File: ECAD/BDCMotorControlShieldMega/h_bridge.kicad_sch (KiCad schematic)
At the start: 23 parts, among them J18 Motor Connector, J19 Limit switch, J8 Limit switch, U14 INA180A1, U7 DRV8870DDA

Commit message: Progressed ECAD.
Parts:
- added C1: 0.1uC, Capacitor_SMD:C_0805_2012Metric_Pad1.18x1.45mm_HandSolder, symbol Device:C
- added U1: 74HC2G08, Package_SO:TSSOP-8_3x3mm_P0.65mm, symbol 74xGxx:74LVC2G08
- renumbered C27 to C10, C38 to C2, C31 to C3, C34 to C4, C36 to C5, C41 to C6, C1 to C7, C33 to C8, C15 to C9, J18 to J10, J19 to J8, J8 to J9, R42 to R1, R43 to R2, R47 to R3, R1 to R4, R39 to R5, R3 to R6, R40 to R7, R31 to R8, R2 to R9, U7 to U2, U14 to U3
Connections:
- net +5V: now also C1.1, U1.8 (VCC), U1.8 (VCC)
- net GND: now also C1.2, U1.4 (GND), U1.4 (GND)
- net PWM1: now also U1.2; no longer U2.3 (IN1)
- net PWM2: now also U1.6; no longer U2.2 (IN2)
- new net: U1.3, U2.2 (IN2)
- new net: U1.7, U2.3 (IN1)
- new net ENABLE_PWM: U1.1, U1.5
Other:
- moved on the sheet: C10, C2, C3, C4, C5, C6, C7, C8, C9, J10, J8, J9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

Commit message: Progressed ECAD.
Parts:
- added U17: 74AHC14, Package_SO:TSSOP-14_4.4x5mm_P0.65mm, symbol 74xx:74HC14
- added U21: 74AHC2G125, Package_SO:TSSOP-8_3x3mm_P0.65mm, symbol 74xGxx:74AUC2G125
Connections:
- net ENCODER_A: now also U21.3; no longer C7.1, R4.1
- net ENCODER_B: now also U21.6; no longer C10.1, R9.1
- net GND: now also U17.7 (GND), U21.4 (GND)
- net LIM1: now also U17.6; no longer C8.1, R5.1
- net LIM2: now also U17.8; no longer C9.1, R6.1
- new net: C8.1, R5.1, U17.5
- new net: C10.1, R9.1, U17.1
- new net: U17.4, U21.2
- new net: U17.12, U21.5
- new net: C9.1, R6.1, U17.9
- new net: U17.10, U17.13
- new net: C7.1, R4.1, U17.11
- new net: U17.2, U17.3
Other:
- moved on the sheet: C10, C3, C4, C5, C7, C8, C9, J8, J9, R4, R5, R6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

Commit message: Progressed ECAD.
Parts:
- removed U1: 74HC2G08, Package_SO:TSSOP-8_3x3mm_P0.65mm, symbol 74xGxx:74LVC2G08
- added C13, C4: 100nC, Capacitor_SMD:C_0805_2012Metric, symbol Device:C
- added U4: 74AHC2G08, Package_SO:TSSOP-8_3x3mm_P0.65mm, symbol 74xGxx:74AUC2G08
- C10: renamed from C4; footprint Capacitor_SMD:C_1210_3225Metric_Pad1.33x2.70mm_HandSolder -> Capacitor_SMD:C_1210_3225Metric
- C12: renamed from C6; value 0.1uC -> 100nC; footprint Capacitor_SMD:C_0805_2012Metric_Pad1.18x1.45mm_HandSolder -> Capacitor_SMD:C_0805_2012Metric; MPN CC0805KRX7R8BB104 -> C0805F104K5RACAUTO
- C14: renamed from C8; MPN (none) -> C0805F104K5RACAUTO
- C15: renamed from C9; MPN (none) -> C0805F104K5RACAUTO
- C5: renamed from C1; value 0.1uC -> 100nC; footprint Capacitor_SMD:C_0805_2012Metric_Pad1.18x1.45mm_HandSolder -> Capacitor_SMD:C_0805_2012Metric; MPN CC0805KRX7R8BB104 -> C0805F104K5RACAUTO
- C6: renamed from C2; value 0.1uC -> 100nC; footprint Capacitor_SMD:C_0805_2012Metric_Pad1.18x1.45mm_HandSolder -> Capacitor_SMD:C_0805_2012Metric; MPN CC0805KRX7R8BB104 -> C0805F104K5RACAUTO
- C7: renamed from C3; value 0.1uC -> 100nC; footprint Capacitor_SMD:C_0805_2012Metric_Pad1.18x1.45mm_HandSolder -> Capacitor_SMD:C_0805_2012Metric; MPN CC0805KRX7R8BB104 -> C0805F104K5RACAUTO
- C8: renamed from C7; footprint Capacitor_SMD:C_0402_1005Metric -> Capacitor_SMD:C_0805_2012Metric
- C9: renamed from C10; footprint Capacitor_SMD:C_0402_1005Metric -> Capacitor_SMD:C_0805_2012Metric
- R10: renamed from R2; footprint Resistor_SMD:R_0805_2012Metric_Pad1.20x1.40mm_HandSolder -> Resistor_SMD:R_0805_2012Metric; MPN RC0805FR-0710KL -> RC0805JR-0710KL
- R11: renamed from R4; footprint Resistor_SMD:R_0402_1005Metric -> Resistor_SMD:R_0805_2012Metric; MPN RC0402FR-071KL -> AC0805FR-7W1KL
- R12: renamed from R9; footprint Resistor_SMD:R_0402_1005Metric -> Resistor_SMD:R_0805_2012Metric; MPN RC0402FR-071KL -> AC0805FR-7W1KL
- R14: renamed from R5; footprint Capacitor_SMD:C_0805_2012Metric -> Resistor_SMD:R_0805_2012Metric; MPN (none) -> RC0805JR-0710KL
- R15: renamed from R6; footprint Capacitor_SMD:C_0805_2012Metric -> Resistor_SMD:R_0805_2012Metric; MPN (none) -> RC0805JR-0710KL
- R16: renamed from R7; footprint Capacitor_SMD:C_0805_2012Metric -> Resistor_SMD:R_0805_2012Metric; MPN (none) -> RC0805JR-0710KL
- R17: renamed from R8; footprint Capacitor_SMD:C_0805_2012Metric -> Resistor_SMD:R_0805_2012Metric; MPN (none) -> RC0805JR-0710KL
- R9: renamed from R1; footprint Resistor_SMD:R_0805_2012Metric_Pad1.20x1.40mm_HandSolder -> Resistor_SMD:R_0805_2012Metric; MPN RC0805FR-0710KL -> RC0805JR-0710KL
- renumbered C5 to C11, J8 to J10, J9 to J11, J10 to J9, R3 to R13, U21 to U3, U17 to U5, U2 to U6, U3 to U7
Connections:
- net +5V: now also U3.8 (VCC), U5.14 (VCC), C13.1, C4.1, U4.8 (VCC)
- net ENABLE_PWM: now also U4.1, U4.5
- net GND: now also C13.2, C4.2, U4.4 (GND)
- net PWM1: now also U4.2
- net PWM2: now also U4.6
- net ~{ENABLE_ENCODER}: now reaches U3.1
- net ~{ENABLE_ENCODER}: now also U3.7
- net at U6.2 (IN2): now also U4.3
- net at U6.3 (IN1): now also U4.7
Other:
- moved on the sheet: C10, C11, C12, C5, C6, C7, C8, C9, J9, R10, R11, R12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

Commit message: Progressed ECAD.
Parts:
- added C14: 100nC, Capacitor_SMD:C_0805_2012Metric, symbol Device:C
- added L1: 10uL, Inductor_SMD:L_0805_2012Metric, symbol Device:L
- renumbered C8 to C10, C9 to C11, C11 to C12, C12 to C13, C13 to C15, C14 to C16, C15 to C17, C4 to C5, C5 to C6, C6 to C7, C7 to C8, C10 to C9
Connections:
- net +5V: now also L1.1; no longer U7.5 (V+)
- net GND: now also C14.2
- new net: C14.1, L1.2, U7.5 (V+)
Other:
- moved on the sheet: C12, C13, C6, C7, C8, C9, R10, R13, R9, U4A, U4B, U4C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

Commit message: Progressed ECAD.
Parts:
- C12, C13, C14, C15, C16, C17, C5, C6, C7, C8, C9, R10, R14, R15, R16, R17, R9: Status (none) -> OK
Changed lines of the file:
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@@
 			)
 		)
+		(property "Status" "OK"
+			(at 27.94 147.32 0)
+			(effects
+				(font
+					(size 1.27 1.27)
+				)
+				(hide yes)
+			)
+		)
 		(pin "1"
 		)
@@
 			)
 		)
+		(property "Status" "OK"
+			(at 160.02 49.53 0)
+			(effects
+				(font
+					(size 1.27 1.27)
+				)
+				(hide yes)
+			)
+		)
 		(pin "1"
 		)
@@
 			)
 		)
+		(property "Status" "OK"
+			(at 191.77 118.11 0)
+			(effects
+				(font
+					(size 1.27 1.27)
+				)
+				(hide yes)
+			)
+		)
 		(pin "1"
 		)
@@
 			)
 		)
+		(property "Status" "OK"
+			(at 238.76 66.04 90)
+			(effects
+				(font
+					(size 1.27 1.27)
+				)
+				(hide yes)
+			)
+		)
 		(pin "2"
 		)
@@
 			)
 		)
+		(property "Status" "OK"
+			(at 88.9 83.82 0)
+			(effects
+				(font
+					(size 1.27 1.27)
+				)
+				(hide yes)
+			)
+		)
 		(pin "1"
 		)
@@
 			)
 		)
+		(property "Status" "OK"
+			(at 247.65 60.96 0)
+			(effects
+				(font
+					(size 1.27 1.27)
+				)
+				(hide yes)
+			)
+		)
 		(pin "2"
 		)
@@
 			)
 		)
+		(property "Status" "OK"
+			(at 149.86 49.53 0)
+			(effects
+				(font
+					(size 1.27 1.27)
+				)
+				(hide yes)
+			)
+		)
 		(pin "1"
 		)
@@
 			)
 		)
+		(property "Status" "OK"
+			(at 238.76 33.02 90)
+			(effects
+				(font
+					(size 1.27 1.27)
+				)
+				(hide yes)
+			)
+		)
 		(pin "2"
 		)
@@
 			)
 		)
+		(property "Status" "OK"
+			(at 88.9 73.66 0)
+			(effects
+				(font
+					(size 1.27 1.27)
+				)
+				(hide yes)
+			)
+		)
 		(pin "1"
 		)
@@
 			)
 		)
+		(property "Status" "OK"
+			(at 115.57 29.21 0)
+			(effects
+				(font
+					(size 1.27 1.27)
+				)
+				(hide yes)
+			)
+		)
 		(pin "1"
 		)
@@
 			)
 		)
+		(property "Status" "OK"
+			(at 77.47 83.82 0)
+			(effects
+				(font
+					(size 1.27 1.27)
+				)
+				(hide yes)
+			)
+		)
 		(pin "1"
 		)
@@
 			)
 		)
+		(property "Status" "OK"
+			(at 227.33 71.12 0)
+			(effects
+				(font
+					(size 1.27 1.27)
+				)
+				(hide yes)
+			)
+		)
 		(pin "2"
 		)
@@
 			)
 		)
+		(property "Status" "OK"
+			(at 128.27 29.21 0)
+			(effects
+				(font
+					(size 1.27 1.27)
+				)
+				(hide yes)
+			)
+		)
 		(pin "1"
 		)
@@
 			)
 		)
+		(property "Status" "OK"
+			(at 227.33 38.1 0)
+			(effects
+				(font
+					(size 1.27 1.27)
+				)
+				(hide yes)
+			)
+		)
 		(pin "2"
 		)
@@
 			)
 		)
+		(property "Status" "OK"
+			(at 101.6 29.21 0)
+			(effects
+				(font
+					(size 1.27 1.27)
+				)
+				(hide yes)
+			)
+		)
 		(pin "1"
 		)
@@
 			)
 		)
+		(property "Status" "OK"
+			(at 247.65 27.94 0)
+			(effects
+				(font
+					(size 1.27 1.27)
+				)
+				(hide yes)
+			)
+		)
 		(pin "2"
 		)
@@
 			(at 36.83 77.47 0)
 			(effects
+				(font
+					(size 1.27 1.27)
+				)
+				(hide yes)
+			)
+		)
+		(property "Status" "OK"
+			(at 36.83 77.47 0)
+			(effects

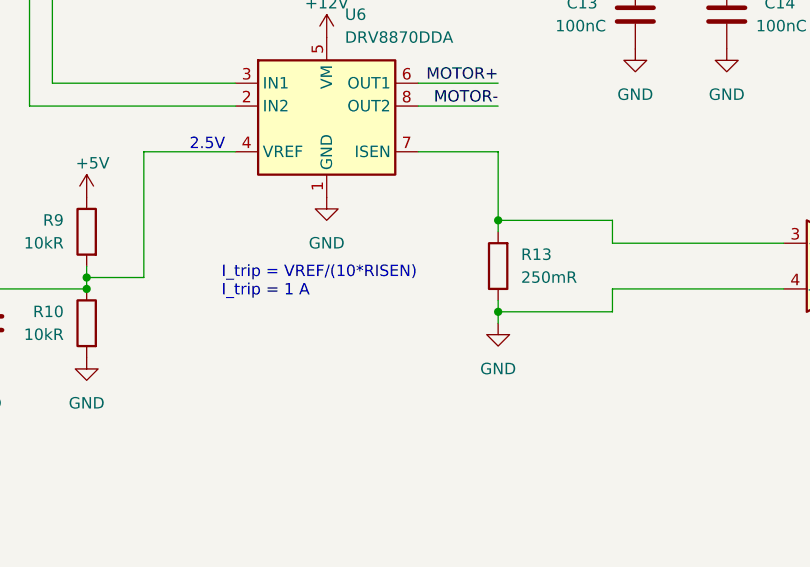
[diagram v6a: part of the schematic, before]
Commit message: Update h_bridge.kicad_sch
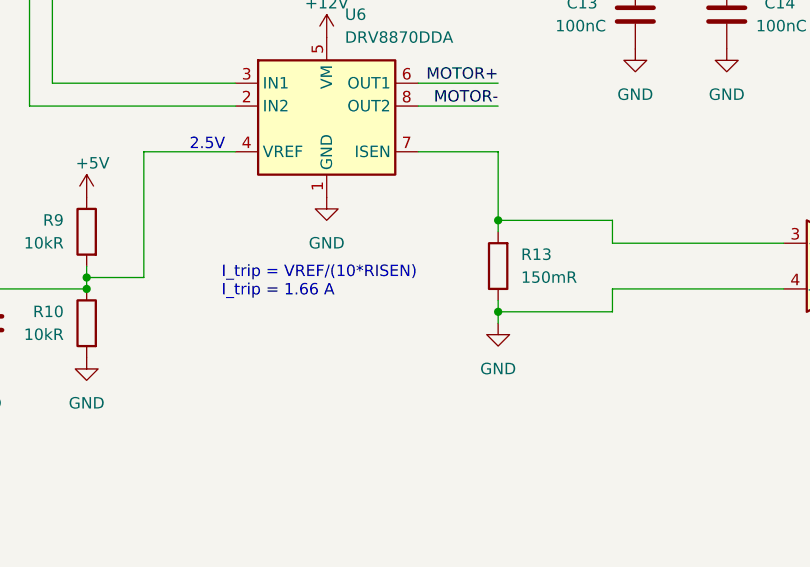
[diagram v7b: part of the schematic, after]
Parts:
- R13: value 250mR -> 150mR; footprint Resistor_SMD:R_2010_5025Metric -> Resistor_SMD:R_1206_3216Metric; MPN RL2010FK-070R25L -> RLH12FTCR150
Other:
- note added: "I_trip = VREF/(10*RISEN) I_trip = 1.66 A"
- note removed: "I_trip = VREF/(10*RISEN) I_trip = 1 A"
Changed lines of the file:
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@@
 		)
 	)
-	(text "I_trip = VREF/(10*RISEN)\nI_trip = 1 A"
+	(text "I_trip = VREF/(10*RISEN)\nI_trip = 1.66 A"
 		(exclude_from_sim no)
 		(at 103.886 81.026 0)
@@
 			)
 		)
-		(property "Value" "250mR"
+		(property "Value" "150mR"
 			(at 137.16 78.7399 0)
 			(effects
@@
 			)
 		)
-		(property "Footprint" "Resistor_SMD:R_2010_5025Metric"
+		(property "Footprint" "Resistor_SMD:R_1206_3216Metric"
 			(at 136.398 77.47 90)
 			(effects
@@
 			)
 		)
-		(property "Datasheet" "https://datasheet.lcsc.com/lcsc/2008171306_YAGEO-RL2010FK-070R25L_C723438.pdf"
+		(property "Datasheet" "https://lcsc.com/datasheet/lcsc_datasheet_2410121306_TA-I-Tech-RLH12FTCR150_C2683383.pdf"
 			(at 134.62 77.47 0)
 			(effects
@@
 			)
 		)
-		(property "MPN" "RL2010FK-070R25L"
+		(property "MPN" "RLH12FTCR150"
 			(at 134.62 77.47 0)
 			(effects

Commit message: Progressed ECAD.
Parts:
- C10, C11: MPN (none) -> CC0805KRX7R9BB101; Status (none) -> OK
- J9: MPN (none) -> B6B-PH-K-S(LF)(SN); Status (none) -> OK
- R11, R12, R13, U3, U4, U5, U6, U7: Status (none) -> OK
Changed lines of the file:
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@@
 			)
 		)
+		(property "Status" "OK"
+			(at 214.63 33.02 0)
+			(effects
+				(font
+					(size 1.27 1.27)
+				)
+				(hide yes)
+			)
+		)
 		(pin "6"
 		)
@@
 			)
 		)
+		(property "Status" "OK"
+			(at 125.73 165.1 90)
+			(effects
+				(font
+					(size 1.27 1.27)
+				)
+				(hide yes)
+			)
+		)
 		(pin "1"
 		)
@@
 			)
 		)
+		(property "Status" "OK"
+			(at 71.12 165.1 0)
+			(effects
+				(font
+					(size 1.27 1.27)
+				)
+				(hide yes)
+			)
+		)
 		(pin "2"
 		)
@@
 			)
 		)
+		(property "Status" "OK"
+			(at 71.12 128.27 0)
+			(effects
+				(font
+					(size 1.27 1.27)
+				)
+				(hide yes)
+			)
+		)
 		(pin "2"
 		)
@@
 			)
 		)
+		(property "Status" "OK"
+			(at 201.93 118.11 0)
+			(effects
+				(font
+					(size 1.27 1.27)
+				)
+				(hide yes)
+			)
+		)
 		(pin "6"
 		)
@@
 			)
 		)
-		(property "Datasheet" "~"
+		(property "Datasheet" "https://lcsc.com/datasheet/lcsc_datasheet_2506131735_YAGEO-CC0805KRX7R9BB101_C107140.pdf"
 			(at 120.65 170.18 0)
 			(effects
@@
 			)
 		)
+		(property "MPN" "CC0805KRX7R9BB101"
+			(at 120.65 170.18 0)
+			(effects
+				(font
+					(size 1.27 1.27)
+				)
+				(hide yes)
+			)
+		)
+		(property "Status" "OK"
+			(at 120.65 170.18 0)
+			(effects
+				(font
+					(size 1.27 1.27)
+				)
+				(hide yes)
+			)
+		)
 		(pin "2"
 		)
@@
 			)
 		)
+		(property "Status" "OK"
+			(at 109.22 128.27 0)
+			(effects
+				(font
+					(size 1.27 1.27)
+				)
+				(hide yes)
+			)
+		)
 		(pin "6"
 		)
@@
 			)
 		)
+		(property "Status" "OK"
+			(at 48.26 77.47 0)
+			(effects
+				(font
+					(size 1.27 1.27)
+				)
+				(hide yes)
+			)
+		)
 		(pin "1"
 		)
@@
 			)
 		)
-		(property "Datasheet" "~"
+		(property "Datasheet" "https://lcsc.com/datasheet/lcsc_datasheet_1811151524_JST-B6B-PH-K-S-LF-SN_C131342.pdf"
 			(at 257.81 116.84 0)
 			(effects
@@
 			)
 		)
-		(property "Status" ""
+		(property "Status" "OK"
+			(at 257.81 116.84 0)
+			(effects
+				(font
+					(size 1.27 1.27)
+				)
+				(hide yes)
+			)
+		)
+		(property "MPN" "B6B-PH-K-S(LF)(SN)"
 			(at 257.81 116.84 0)
 			(effects
@@
 			)
 		)
+		(property "Status" "OK"
+			(at 57.15 27.94 0)
+			(effects
+				(font
+					(size 1.27 1.27)
+				)
+				(hide yes)
+			)
+		)
 		(pin "1"
 		)
@@
 			)
 		)
+		(property "Status" "OK"
+			(at 134.62 77.47 0)
+			(effects
+				(font
+					(size 1.27 1.27)
+				)
+				(hide yes)
+			)
+		)
 		(pin "1"
 		)
@@
 			)
 		)
+		(property "Status" "OK"
+			(at 57.15 45.72 0)
+			(effects
+				(font
+					(size 1.27 1.27)
+				)
+				(hide yes)
+			)
+		)
 		(pin "1"
 		)
@@
 			)
 		)
+		(property "Status" "OK"
+			(at 93.98 128.27 0)
+			(effects
+				(font
+					(size 1.27 1.27)
+				)
+				(hide yes)
+			)
+		)
 		(pin "6"
 		)
@@
 			)
 		)
+		(property "Status" "OK"
+			(at 38.1 147.32 0)
+			(effects
+				(font
+					(size 1.27 1.27)
+				)
+				(hide yes)
+			)
+		)
 		(pin "2"
 		)
@@
 			)
 		)
+		(property "Status" "OK"
+			(at 214.63 66.04 0)
+			(effects
+				(font
+					(size 1.27 1.27)
+				)
+				(hide yes)
+			)
+		)
 		(pin "6"
 		)
@@
 			)
 		)
+		(property "Status" "OK"
+			(at 115.57 59.69 0)
+			(effects
+				(font
+					(size 1.27 1.27)
+				)
+				(hide yes)
+			)
+		)
 		(pin "1"
 		)
@@
 			)
 		)
+		(property "Status" "OK"
+			(at 109.22 165.1 0)
+			(effects
+				(font
+					(size 1.27 1.27)
+				)
+				(hide yes)
+			)
+		)
 		(pin "6"
 		)
@@
 			)
 		)
+		(property "Status" "OK"
+			(at 173.99 77.47 0)
+			(effects
+				(font
+					(size 1.27 1.27)
+				)
+				(hide yes)
+			)
+		)
 		(pin "1"
 		)
@@
 			)
 		)
-		(property "Datasheet" "~"
+		(property "Datasheet" "https://lcsc.com/datasheet/lcsc_datasheet_2506131735_YAGEO-CC0805KRX7R9BB101_C107140.pdf"
 			(at 120.65 133.35 0)
 			(effects
@@
 			)
 		)
+		(property "MPN" "CC0805KRX7R9BB101"
+			(at 120.65 133.35 0)
+			(effects
+				(font
+					(size 1.27 1.27)
+				)
+				(hide yes)
+			)
+		)
+		(property "Status" "OK"
+			(at 120.65 133.35 0)
+			(effects
+				(font
+					(size 1.27 1.27)
+				)
+				(hide yes)
+			)
+		)
 		(pin "2"
 		)
@@
 			)
 		)
+		(property "Status" "OK"
+			(at 93.98 165.1 0)
+			(effects
+				(font
+					(size 1.27 1.27)
+				)
+				(hide yes)
+			)
+		)
 		(pin "6"
 		)
@@
 			(at 125.73 128.27 90)
 			(effects
+				(font
+					(size 1.27 1.27)
+				)
+				(hide yes)
+			)
+		)
+		(property "Status" "OK"
+			(at 125.73 128.27 90)
+			(effects
